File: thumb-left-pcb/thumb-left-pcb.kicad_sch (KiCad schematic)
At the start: 25 parts, among them J1 Conn_01x10

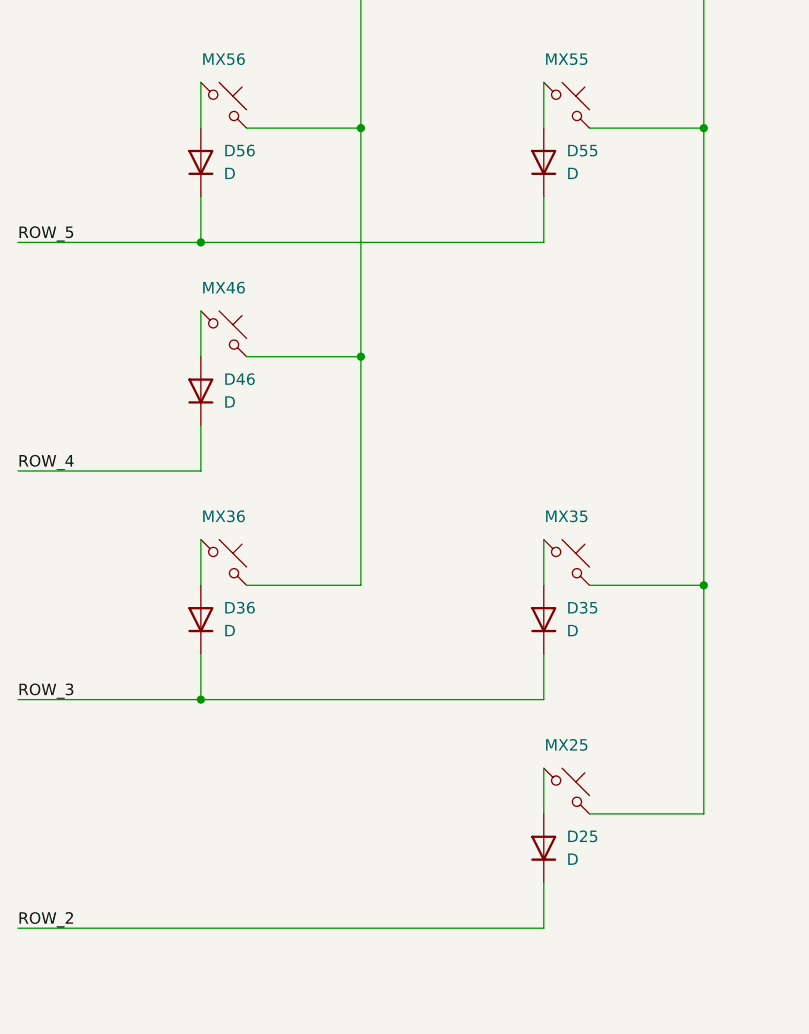
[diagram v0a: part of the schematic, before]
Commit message: update left footprints
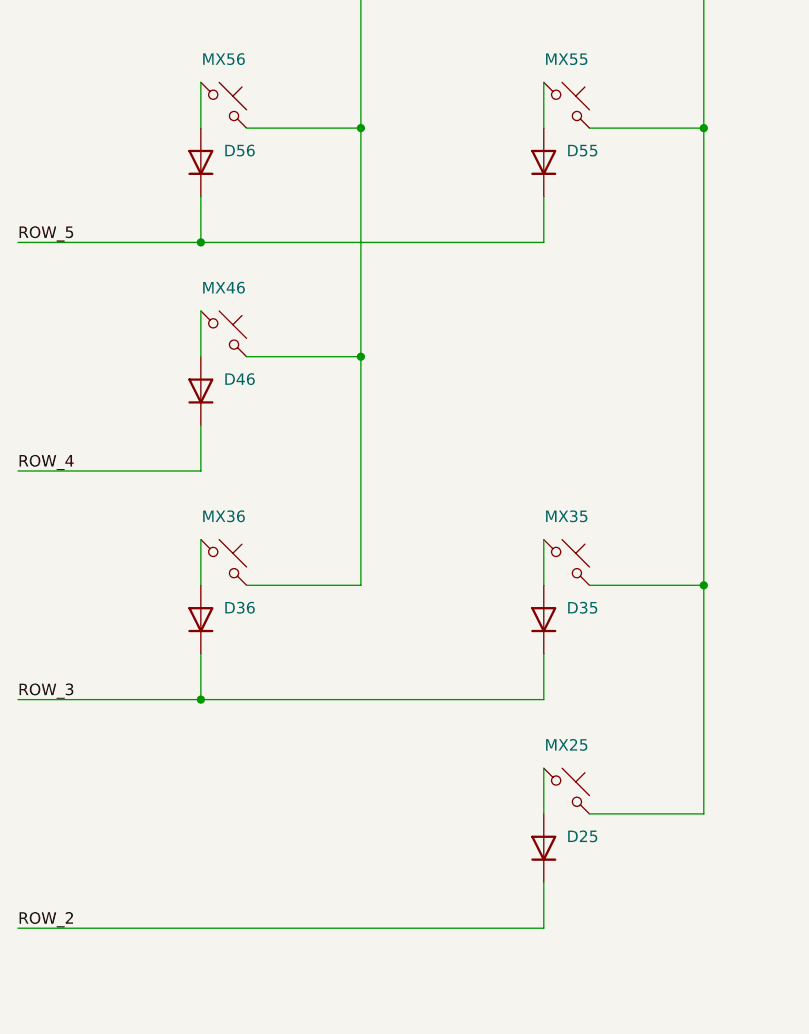
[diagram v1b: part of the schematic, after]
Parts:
- C25, C35, C36, C46, C55, C56: footprint (none) -> Capacitor_SMD:C_0805_2012Metric_Pad1.18x1.45mm_HandSolder
- D25, D35, D36, D46, D55, D56: value D -> 1N4148WL; footprint (none) -> Diode_SMD:D_SOD-123F
- J1: footprint (none) -> Connector_PinHeader_2.54mm:PinHeader_1x10_P2.54mm_Vertical
- MX25, MX35, MX55, MX56: footprint PCM_marbastlib-mx:SW_MX_HS_CPG151101S11_1u -> PCM_Switch_Keyboard_Cherry_MX:SW_Cherry_MX_PCB_1.00u
- MX36, MX46: footprint PCM_marbastlib-mx:SW_MX_HS_CPG151101S11_1u -> PCM_Switch_Keyboard_Cherry_MX:SW_Cherry_MX_PCB_2.00u_90deg
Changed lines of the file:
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@@
 			)
 		)
-		(property "Footprint" ""
+		(property "Footprint" "Capacitor_SMD:C_0805_2012Metric_Pad1.18x1.45mm_HandSolder"
 			(at 178.7652 113.03 0)
 			(effects
@@
 			)
 		)
-		(property "Datasheet" "~"
+		(property "Datasheet" "https://www.yageogroup.com/content/datasheet/asset/file/KEM_C1002_X7R_SMD"
 			(at 177.8 109.22 0)
 			(effects
@@
 			)
 		)
-		(property "Footprint" ""
+		(property "Footprint" "Capacitor_SMD:C_0805_2012Metric_Pad1.18x1.45mm_HandSolder"
 			(at 199.0852 62.23 0)
 			(effects
@@
 			)
 		)
-		(property "Datasheet" "~"
+		(property "Datasheet" "https://www.yageogroup.com/content/datasheet/asset/file/KEM_C1002_X7R_SMD"
 			(at 198.12 58.42 0)
 			(effects
@@
 			)
 		)
-		(property "Footprint" ""
+		(property "Footprint" "Capacitor_SMD:C_0805_2012Metric_Pad1.18x1.45mm_HandSolder"
 			(at 178.7652 62.23 0)
 			(effects
@@
 			)
 		)
-		(property "Datasheet" "~"
+		(property "Datasheet" "https://www.yageogroup.com/content/datasheet/asset/file/KEM_C1002_X7R_SMD"
 			(at 177.8 58.42 0)
 			(effects
@@
 			)
 		)
-		(property "Value" "D"
+		(property "Value" "1N4148WL"
 			(at 101.6 110.4899 90)
 			(effects
@@
 				)
 				(justify right)
-			)
-		)
-		(property "Footprint" ""
+				(hide yes)
+			)
+		)
+		(property "Footprint" "Diode_SMD:D_SOD-123F"
 			(at 99.06 109.22 0)
 			(effects
@@
 			)
 		)
-		(property "Datasheet" "~"
+		(property "Datasheet" "https://mm.digikey.com/Volume0/opasdata/d220001/medias/docus/7158/5272_1N4148WL.pdf"
 			(at 99.06 109.22 0)
 			(effects
@@
 			)
 		)
-		(property "Footprint" "PCM_marbastlib-mx:SW_MX_HS_CPG151101S11_1u"
+		(property "Footprint" "PCM_Switch_Keyboard_Cherry_MX:SW_Cherry_MX_PCB_2.00u_90deg"
 			(at 63.5 102.87 0)
 			(effects
@@
 			)
 		)
-		(property "Footprint" ""
+		(property "Footprint" "Connector_PinHeader_2.54mm:PinHeader_1x10_P2.54mm_Vertical"
 			(at 106.68 171.45 0)
 			(effects
@@
 			)
 		)
-		(property "Value" "D"
+		(property "Value" "1N4148WL"
 			(at 101.6 59.6899 90)
 			(effects
@@
 				)
 				(justify right)
-			)
-		)
-		(property "Footprint" ""
+				(hide yes)
+			)
+		)
+		(property "Footprint" "Diode_SMD:D_SOD-123F"
 			(at 99.06 58.42 0)
 			(effects
@@
 			)
 		)
-		(property "Datasheet" "~"
+		(property "Datasheet" "https://mm.digikey.com/Volume0/opasdata/d220001/medias/docus/7158/5272_1N4148WL.pdf"
 			(at 99.06 58.42 0)
 			(effects
@@
 			)
 		)
-		(property "Value" "D"
+		(property "Value" "1N4148WL"
 			(at 63.5 85.0899 90)
 			(effects
@@
 				)
 				(justify right)
-			)
-		)
-		(property "Footprint" ""
+				(hide yes)
+			)
+		)
+		(property "Footprint" "Diode_SMD:D_SOD-123F"
 			(at 60.96 83.82 0)
 			(effects
@@
 			)
 		)
-		(property "Datasheet" "~"
+		(property "Datasheet" "https://mm.digikey.com/Volume0/opasdata/d220001/medias/docus/7158/5272_1N4148WL.pdf"
 			(at 60.96 83.82 0)
 			(effects
@@
 			)
 		)
-		(property "Footprint" ""
+		(property "Footprint" "Capacitor_SMD:C_0805_2012Metric_Pad1.18x1.45mm_HandSolder"
 			(at 199.0852 138.43 0)
 			(effects
@@
 			)
 		)
-		(property "Datasheet" "~"
+		(property "Datasheet" "https://www.yageogroup.com/content/datasheet/asset/file/KEM_C1002_X7R_SMD"
 			(at 198.12 134.62 0)
 			(effects
@@
 			)
 		)
-		(property "Footprint" ""
+		(property "Footprint" "Capacitor_SMD:C_0805_2012Metric_Pad1.18x1.45mm_HandSolder"
 			(at 178.7652 87.63 0)
 			(effects
@@
 			)
 		)
-		(property "Datasheet" "~"
+		(property "Datasheet" "https://www.yageogroup.com/content/datasheet/asset/file/KEM_C1002_X7R_SMD"
 			(at 177.8 83.82 0)
 			(effects
@@
 			)
 		)
-		(property "Footprint" "PCM_marbastlib-mx:SW_MX_HS_CPG151101S11_1u"
+		(property "Footprint" "PCM_Switch_Keyboard_Cherry_MX:SW_Cherry_MX_PCB_1.00u"
 			(at 101.6 102.87 0)
 			(effects
@@
 			)
 		)
-		(property "Footprint" "PCM_marbastlib-mx:SW_MX_HS_CPG151101S11_1u"
+		(property "Footprint" "PCM_Switch_Keyboard_Cherry_MX:SW_Cherry_MX_PCB_1.00u"
 			(at 101.6 128.27 0)
 			(effects
@@
 			)
 		)
-		(property "Footprint" "PCM_marbastlib-mx:SW_MX_HS_CPG151101S11_1u"
+		(property "Footprint" "PCM_Switch_Keyboard_Cherry_MX:SW_Cherry_MX_PCB_1.00u"
 			(at 63.5 52.07 0)
 			(effects
@@
 			)
 		)
-		(property "Footprint" ""
+		(property "Footprint" "Capacitor_SMD:C_0805_2012Metric_Pad1.18x1.45mm_HandSolder"
 			(at 199.0852 113.03 0)
 			(effects
@@
 			)
 		)
-		(property "Datasheet" "~"
+		(property "Datasheet" "https://www.yageogroup.com/content/datasheet/asset/file/KEM_C1002_X7R_SMD"
 			(at 198.12 109.22 0)
 			(effects
@@
 			)
 		)
-		(property "Value" "D"
+		(property "Value" "1N4148WL"
 			(at 63.5 59.6899 90)
 			(effects
@@
 				)
 				(justify right)
-			)
-		)
-		(property "Footprint" ""
+				(hide yes)
+			)
+		)
+		(property "Footprint" "Diode_SMD:D_SOD-123F"
 			(at 60.96 58.42 0)
 			(effects
@@
 			)
 		)
-		(property "Datasheet" "~"
+		(property "Datasheet" "https://mm.digikey.com/Volume0/opasdata/d220001/medias/docus/7158/5272_1N4148WL.pdf"
 			(at 60.96 58.42 0)
 			(effects
@@
 			)
 		)
-		(property "Value" "D"
+		(property "Value" "1N4148WL"
 			(at 101.6 135.8899 90)
 			(effects
@@
 				)
 				(justify right)
-			)
-		)
-		(property "Footprint" ""
+				(hide yes)
+			)
+		)
+		(property "Footprint" "Diode_SMD:D_SOD-123F"
 			(at 99.06 134.62 0)
 			(effects
@@
 			)
 		)
-		(property "Datasheet" "~"
+		(property "Datasheet" "https://mm.digikey.com/Volume0/opasdata/d220001/medias/docus/7158/5272_1N4148WL.pdf"
 			(at 99.06 134.62 0)
 			(effects
@@
 			)
 		)
-		(property "Footprint" "PCM_marbastlib-mx:SW_MX_HS_CPG151101S11_1u"
+		(property "Footprint" "PCM_Switch_Keyboard_Cherry_MX:SW_Cherry_MX_PCB_2.00u_90deg"
 			(at 63.5 77.47 0)
 			(effects
@@
 			)
 		)
-		(property "Footprint" "PCM_marbastlib-mx:SW_MX_HS_CPG151101S11_1u"
+		(property "Footprint" "PCM_Switch_Keyboard_Cherry_MX:SW_Cherry_MX_PCB_1.00u"
 			(at 101.6 52.07 0)
 			(effects
@@
 			)
 		)
-		(property "Value" "D"
+		(property "Value" "1N4148WL"
 			(at 63.5 110.4899 90)
 			(effects
@@
 				)
 				(justify right)
-			)
-		)
-		(property "Footprint" ""
+				(hide yes)
+			)
+		)
+		(property "Footprint" "Diode_SMD:D_SOD-123F"
 			(at 60.96 109.22 0)
 			(effects
@@
 			)
 		)
-		(property "Datasheet" "~"
+		(property "Datasheet" "https://mm.digikey.com/Volume0/opasdata/d220001/medias/docus/7158/5272_1N4148WL.pdf"
 			(at 60.96 109.22 0)
 			(effects

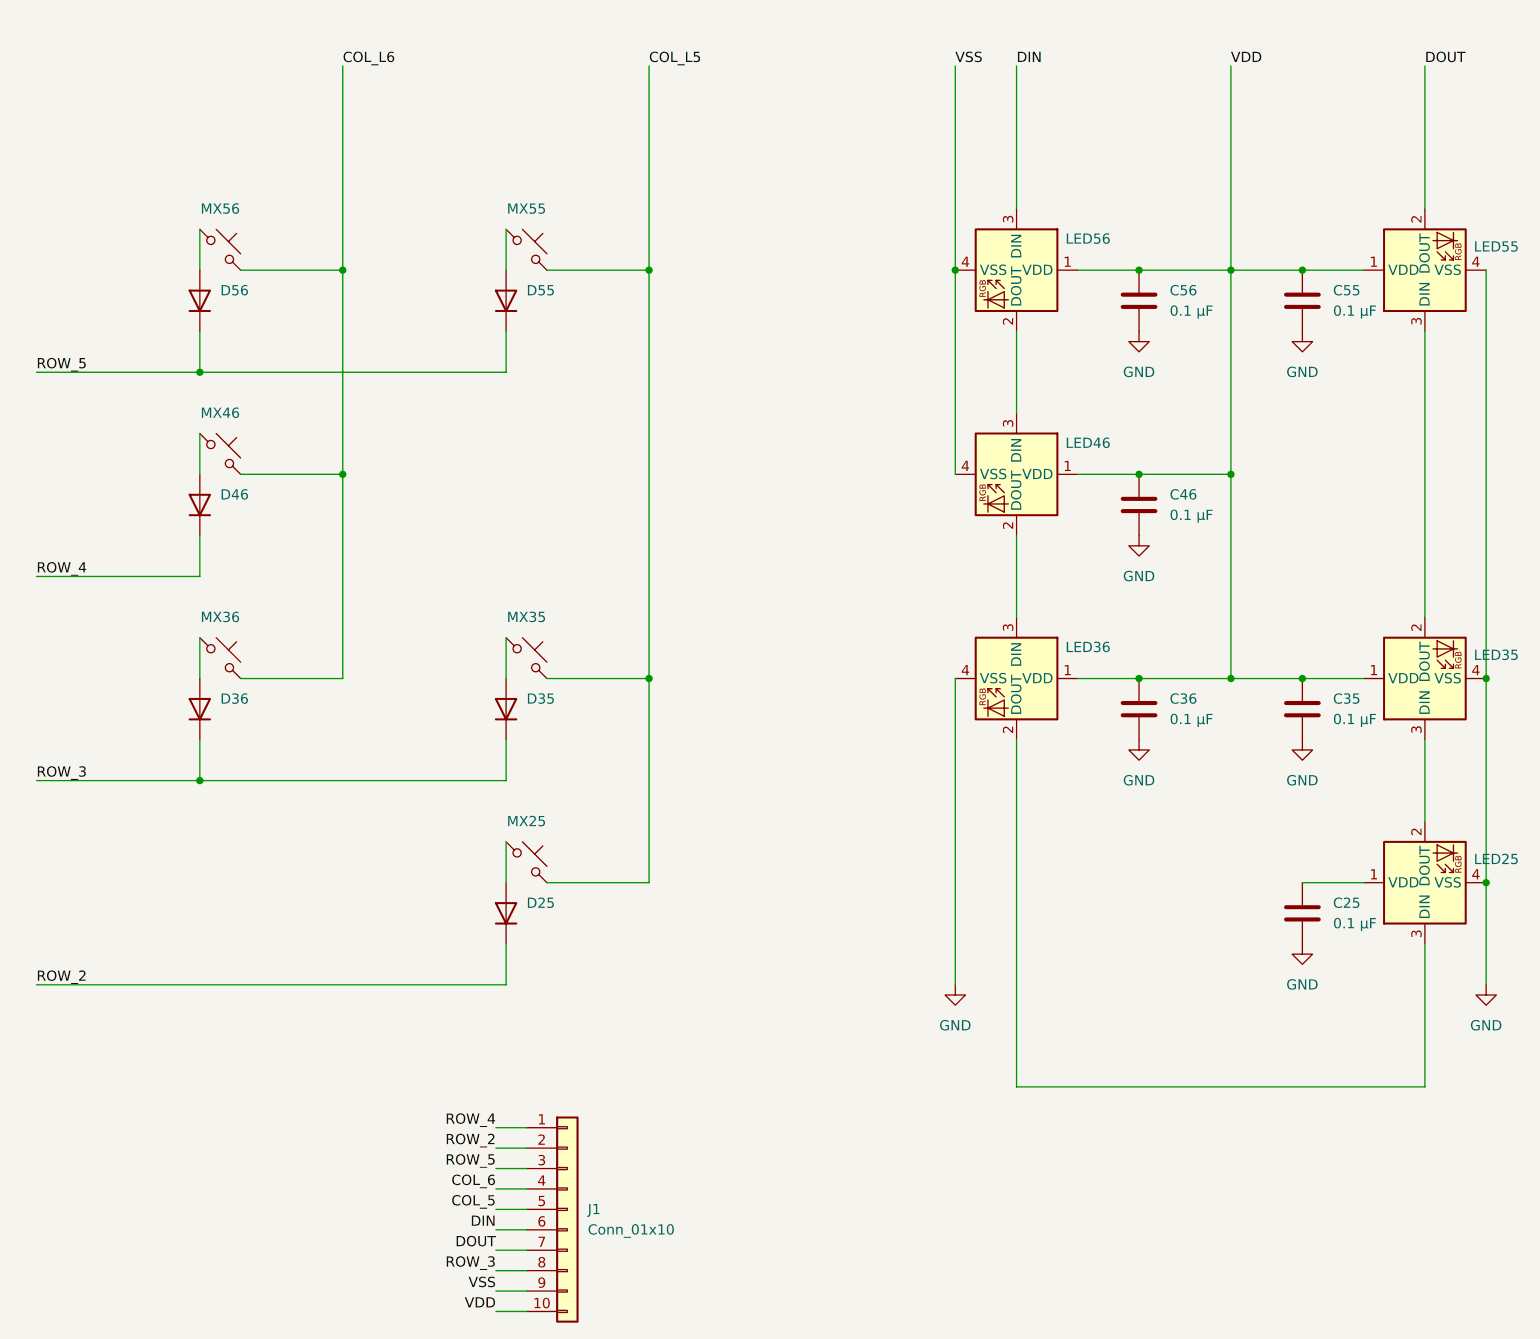
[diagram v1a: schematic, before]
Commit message: rework left-thumb schematic
The uuid's match up so that when the pcb is layed out
the right can be used as a starting point.
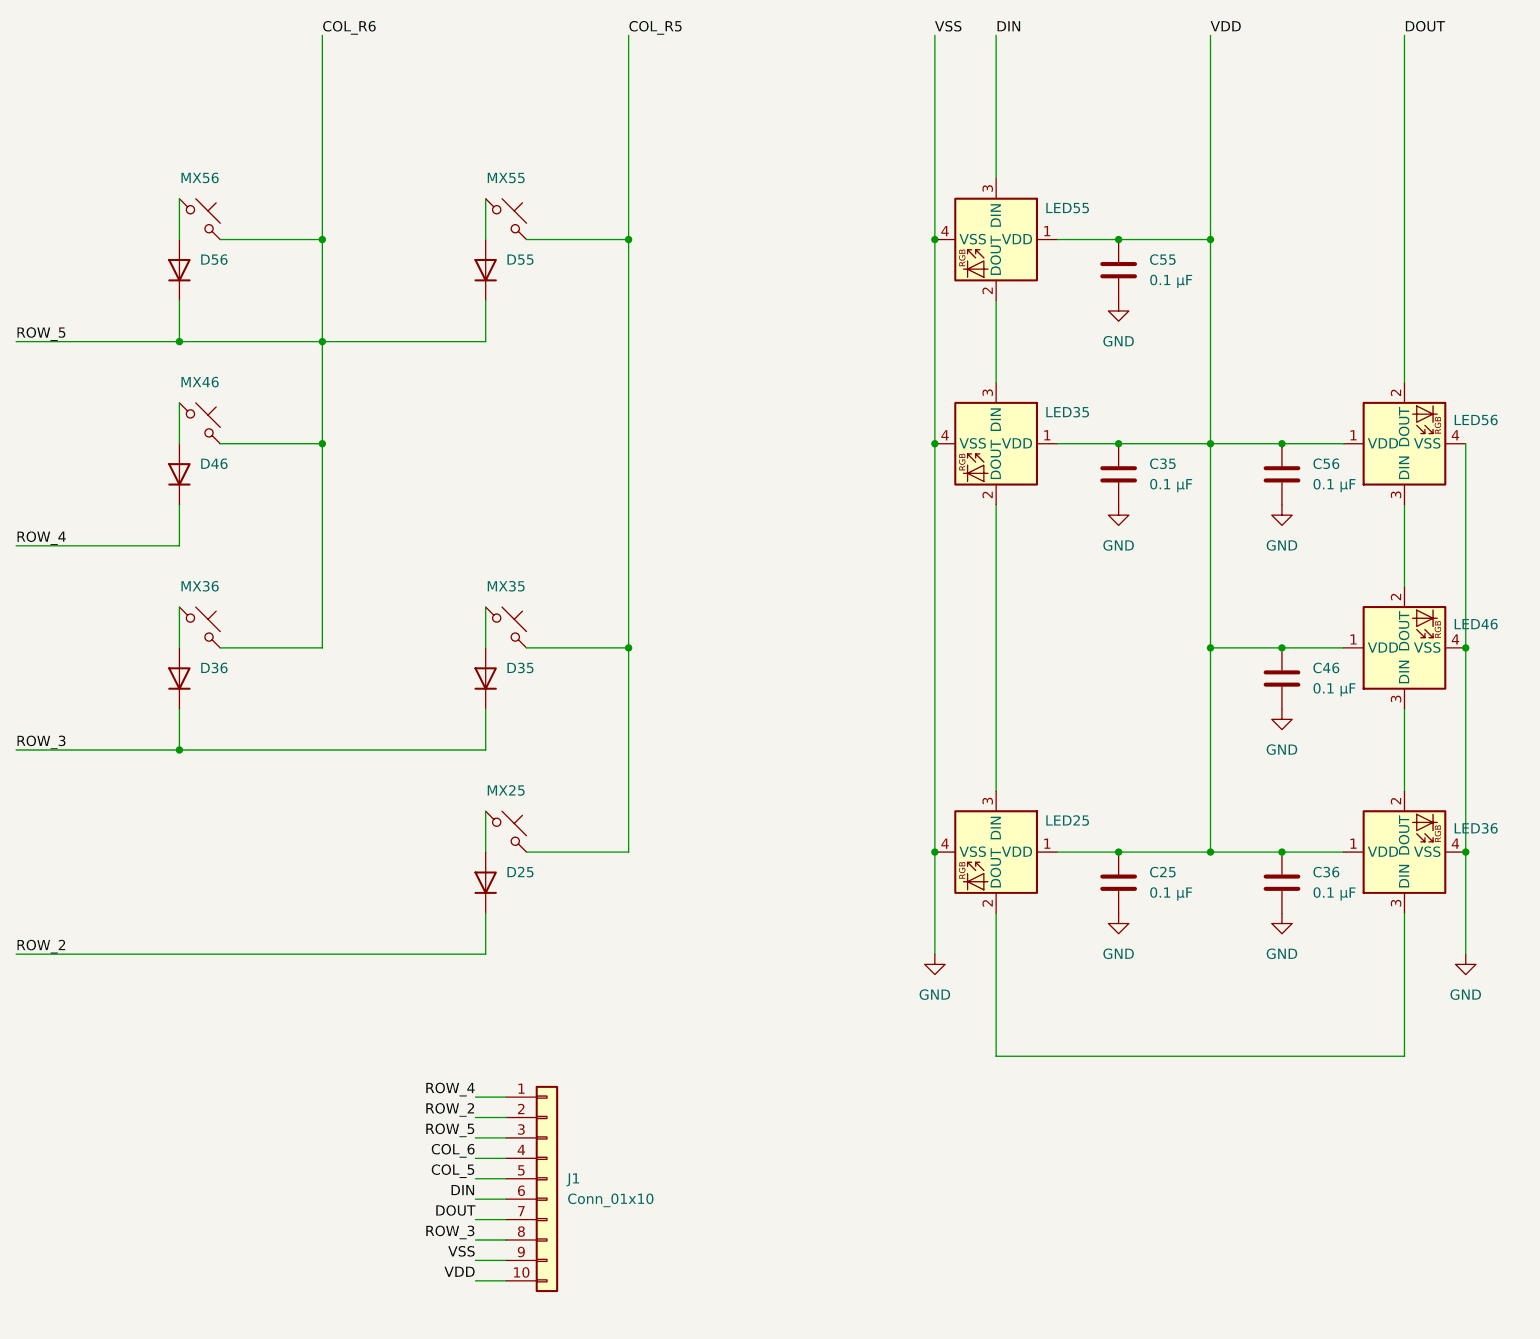
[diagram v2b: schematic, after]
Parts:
- MX25: renamed from MX36; footprint PCM_Switch_Keyboard_Cherry_MX:SW_Cherry_MX_PCB_2.00u_90deg -> PCM_Switch_Keyboard_Cherry_MX:SW_Cherry_MX_PCB_1.00u
- MX35: renamed from MX46; footprint PCM_Switch_Keyboard_Cherry_MX:SW_Cherry_MX_PCB_2.00u_90deg -> PCM_Switch_Keyboard_Cherry_MX:SW_Cherry_MX_PCB_1.00u
- MX36: renamed from MX25; footprint PCM_Switch_Keyboard_Cherry_MX:SW_Cherry_MX_PCB_1.00u -> PCM_Switch_Keyboard_Cherry_MX:SW_Cherry_MX_PCB_2.00u_90deg
- MX46: renamed from MX35; footprint PCM_Switch_Keyboard_Cherry_MX:SW_Cherry_MX_PCB_1.00u -> PCM_Switch_Keyboard_Cherry_MX:SW_Cherry_MX_PCB_2.00u_90deg
- renumbered C36 to C25, C46 to C35, C25 to C36, C35 to C46, C56 to C55, C55 to C56, D36 to D25, D46 to D35, D25 to D36, D35 to D46, D56 to D55, D55 to D56, LED36 to LED25, LED46 to LED35, LED25 to LED36, LED35 to LED46, LED56 to LED55, LED55 to LED56, MX56 to MX55, MX55 to MX56
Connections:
- net ROW_5 is gone; now on net COL_R6: D55.1 (K), D56.1 (K), J1.3 (Pin_3)
- net VSS is gone; now on net GND: J1.9 (Pin_9), LED35.4 (VSS), LED55.4 (VSS)
- net ROW_2: now also D25.1 (K); no longer D36.1 (K)
- net ROW_3: now also D35.1 (K), D36.1 (K); no longer D25.1 (K), D46.1 (K)
- net ROW_4: now also D46.1 (K); no longer D35.1 (K)
- net VDD: now also C36.1, LED36.1 (VDD)
- net COL_L5 renamed COL_R6
- net COL_L6 renamed COL_R5
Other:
- moved on the sheet: C25, C35, C36, C46, C55, C56, D25, D35, D36, D46, D55, D56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
